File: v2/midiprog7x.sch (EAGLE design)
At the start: 58 parts, among them IC1 PIC18F4550_40, IC2 TPIC6B596N, IC3 78L05Z, IC4 TPIC6B596N, Q1 8MHz, Q2 2N2222A, Q3 2N2222A, Q4 2N2222A

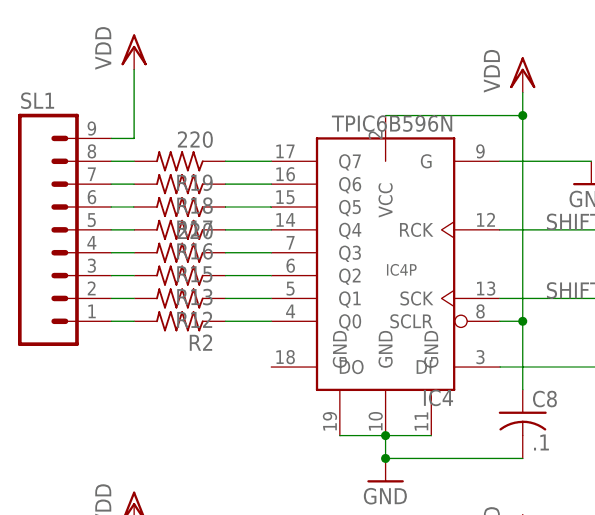
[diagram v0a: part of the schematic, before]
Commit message: Added resistor values.
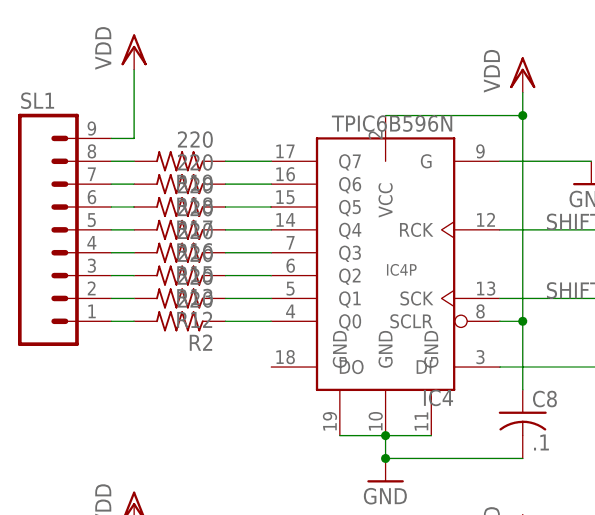
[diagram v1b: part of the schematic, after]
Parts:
- R12, R13, R16, R17, R18, R2: value (none) -> 220
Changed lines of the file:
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@@
 <part name="VDD8" library="supply1" deviceset="VDD" device=""/>
 <part name="GND10" library="supply1" deviceset="GND" device=""/>
-<part name="R2" library="rcl" deviceset="R-US_" device="0207/10"/>
-<part name="R12" library="rcl" deviceset="R-US_" device="0207/10"/>
-<part name="R13" library="rcl" deviceset="R-US_" device="0207/10"/>
+<part name="R2" library="rcl" deviceset="R-US_" device="0207/10" value="220"/>
+<part name="R12" library="rcl" deviceset="R-US_" device="0207/10" value="220"/>
+<part name="R13" library="rcl" deviceset="R-US_" device="0207/10" value="220"/>
 <part name="R15" library="rcl" deviceset="R-US_" device="0207/10" value="220"/>
 <part name="GND14" library="supply1" deviceset="GND" device=""/>
 <part name="C8" library="rcl" deviceset="C-US" device="050-025X075" value=".1"/>
 <part name="VDD12" library="supply1" deviceset="VDD" device=""/>
-<part name="R16" library="rcl" deviceset="R-US_" device="0207/10"/>
-<part name="R17" library="rcl" deviceset="R-US_" device="0207/10"/>
-<part name="R18" library="rcl" deviceset="R-US_" device="0207/10"/>
+<part name="R16" library="rcl" deviceset="R-US_" device="0207/10" value="220"/>
+<part name="R17" library="rcl" deviceset="R-US_" device="0207/10" value="220"/>
+<part name="R18" library="rcl" deviceset="R-US_" device="0207/10" value="220"/>
 <part name="R19" library="rcl" deviceset="R-US_" device="0207/10" value="220"/>
 <part name="R20" library="rcl" deviceset="R-US_" device="0207/10"/>

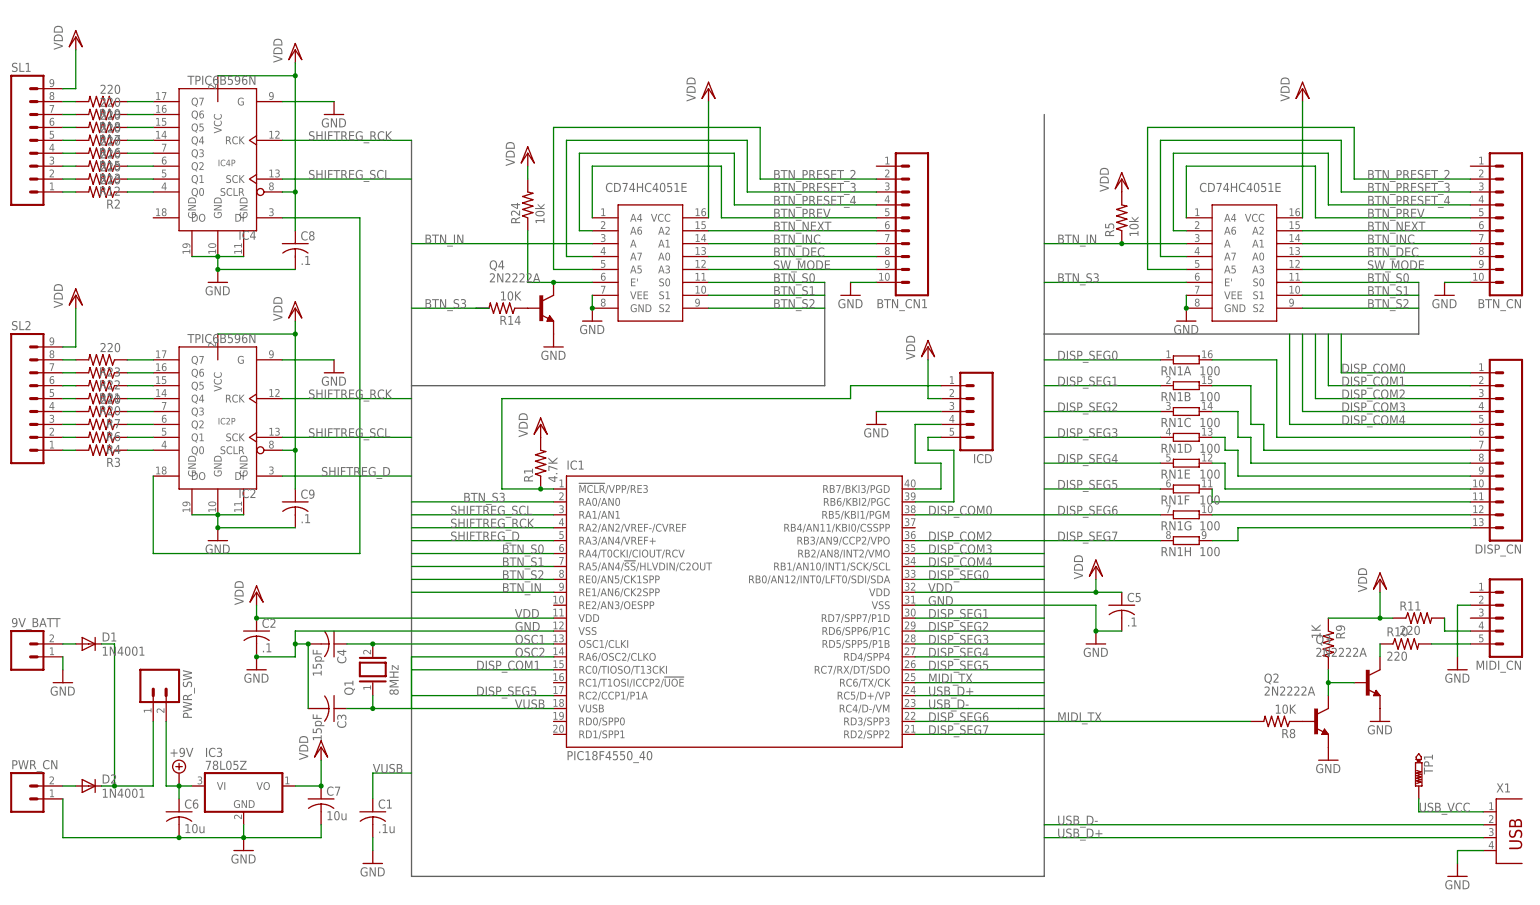
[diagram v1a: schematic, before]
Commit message: Removed busses; corrected names on button inputs; fixed almost all ERC errors.
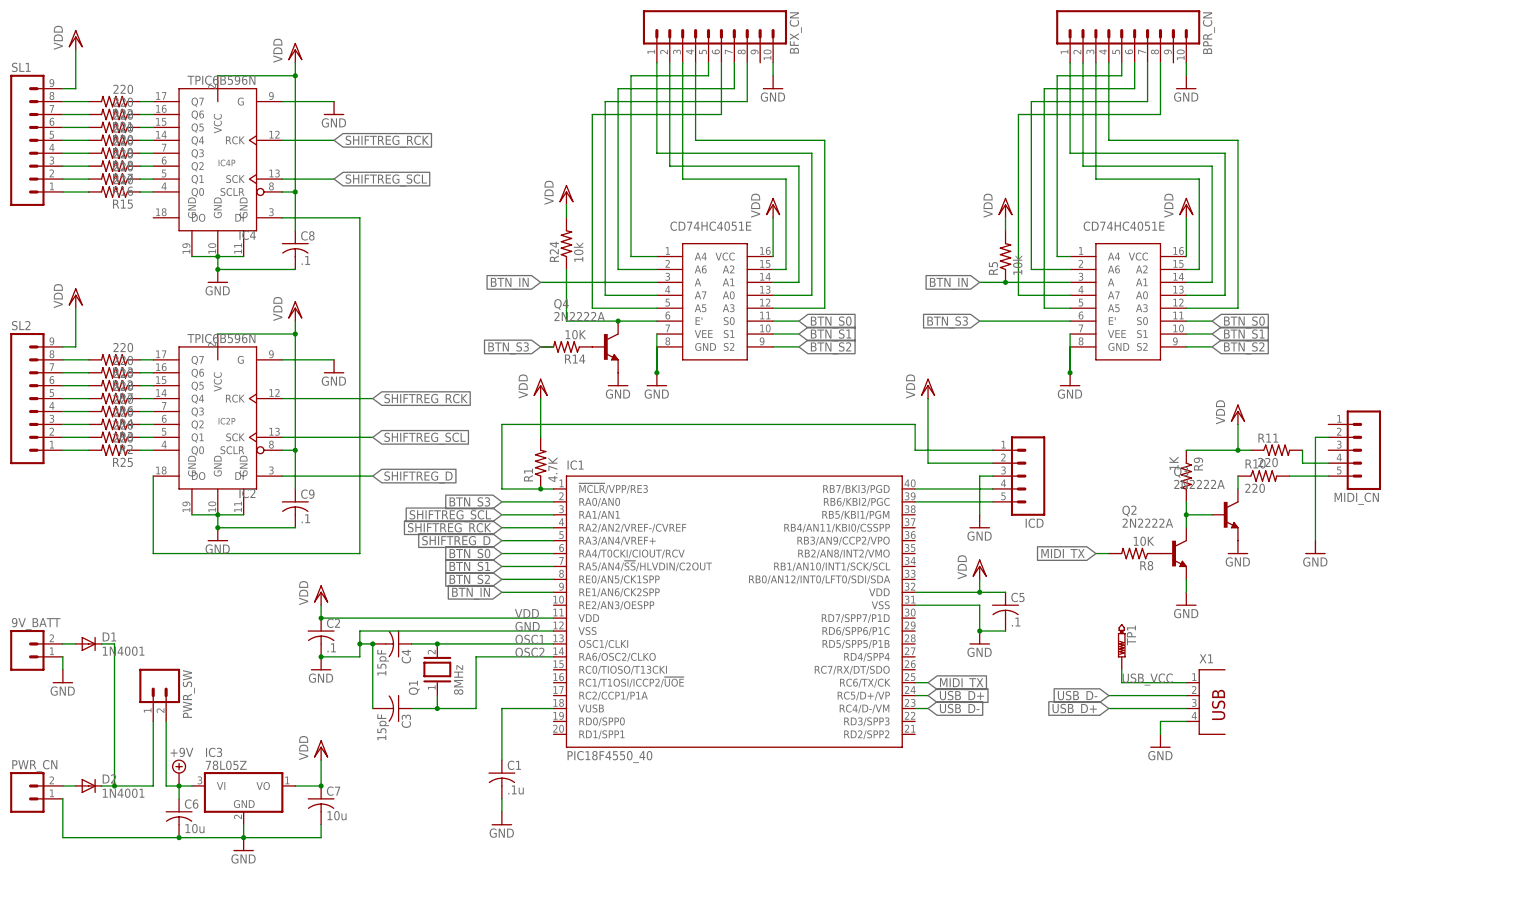
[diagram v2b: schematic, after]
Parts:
- removed BTN_CN, BTN_CN1: (no value), con-amp-quick:M10
- removed DISP_CN: (no value), con-amp-quick:M13
- removed R23: 220, rcl:R-US_0207/10
- removed RN1: 100, resistor-dil:8R-N
- added BFX_CN, BPR_CN: (no value), con-amp-quick:M10
- added R25: 220, rcl:R-US_0207/10
- R20, R21, R22, R3, R4, R6: value (none) -> 220
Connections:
- net VUSB renamed N$18
- removed net BTN_DEC: BTN_CN.8, BTN_CN1.8, U$1.A0, U$2.A0
- removed net BTN_INC: BTN_CN.7, BTN_CN1.7, U$1.A1, U$2.A1
- removed net BTN_NEXT: BTN_CN.6, BTN_CN1.6, U$1.A2, U$2.A2
- removed net BTN_PRESET_2: BTN_CN.2, BTN_CN1.2, U$1.A5, U$2.A5
- removed net BTN_PRESET_3: BTN_CN.3, BTN_CN1.3, U$1.A7, U$2.A7
- removed net BTN_PRESET_4: BTN_CN.4, BTN_CN1.4, U$1.A6, U$2.A6
- removed net BTN_PREV: BTN_CN.5, BTN_CN1.5, U$1.A4, U$2.A4
- removed net DISP_COM0: DISP_CN.1, IC1.RB5/KBI1/PGM
- removed net DISP_COM1: DISP_CN.2, IC1.RC0/TIOSO/T13CKI
- removed net DISP_COM2: DISP_CN.3, IC1.RB3/AN9/CCP2/VPO
- removed net DISP_COM3: DISP_CN.4, IC1.RB2/AN8/INT2/VMO
- removed net DISP_COM4: DISP_CN.5, IC1.RB1/AN10/INT1/SCK/SCL
- removed net DISP_SEG0: IC1.RB0/AN12/INT0/LFT0/SDI/SDA, RN1A.1
- removed net DISP_SEG1: IC1.RD7/SPP7/P1D, RN1B.1
- removed net DISP_SEG2: IC1.RD6/SPP6/P1C, RN1C.1
- removed net DISP_SEG3: IC1.RD5/SPP5/P1B, RN1D.1
- removed net DISP_SEG4: IC1.RD4/SPP4, RN1E.1
- removed net DISP_SEG5: IC1.RC2/CCP1/P1A, IC1.RC7/RX/DT/SDO, RN1F.1
- removed net DISP_SEG6: IC1.RD3/SPP3, RN1G.1
- removed net DISP_SEG7: IC1.RD2/SPP2, RN1H.1
- removed net N$16 (its old number): DISP_CN.13, RN1H.2
- removed net N$17 (its old number): DISP_CN.12, RN1G.2
- removed net N$18 (its old number): DISP_CN.11, RN1F.2
- removed net N$46: R20.1
- removed net N$47: R21.1
- removed net N$48: R22.1
- removed net N$49: R23.1
- removed net N$50: R23.2, SL2.8
- removed net SW_MODE: BTN_CN.9, BTN_CN1.9, U$1.A3, U$2.A3
- new net BFX1: BFX_CN.1, U$2.A0
- new net BFX2: BFX_CN.2, U$2.A1
- new net BFX3: BFX_CN.3, U$2.A2
- new net BFX4: BFX_CN.4, U$2.A3
- new net BFX5: BFX_CN.5, U$2.A4
- new net BFX6: BFX_CN.6, U$2.A5
- new net BFX7: BFX_CN.7, U$2.A6
- new net BFX8: BFX_CN.8, U$2.A7
- new net BPR1: BPR_CN.1, U$1.A0
- new net BPR2: BPR_CN.2, U$1.A1
- new net BPR3: BPR_CN.3, U$1.A2
- new net BPR4: BPR_CN.4, U$1.A3
- new net BPR5: BPR_CN.5, U$1.A4
- new net BPR6: BPR_CN.6, U$1.A5
- new net BPR7: BPR_CN.7, U$1.A6
- new net BPR8: BPR_CN.8, U$1.A7
- net GND: now also BFX_CN.10, BPR_CN.10; no longer BTN_CN.10, BTN_CN1.10
- net N$10: now also IC4G$1.Q6, R21.1; no longer R12.2, SL1.2
- net N$11: now also R21.2, SL1.7; no longer R13.2, SL1.3
- net N$12: now also R20.2, SL1.6; no longer IC4G$1.Q0, R2.1
- net N$13: now also IC4G$1.Q5, R20.1; no longer IC4G$1.Q1, R12.1
- net N$14: now also IC4G$1.Q4, R19.1; no longer IC4G$1.Q2, R13.1
- net N$15: now also R18.1; no longer R15.1
- net N$19: now also R19.2, SL1.5; no longer DISP_CN.10, RN1E.2
- net N$2: now also R22.2, SL1.8; no longer R2.2, SL1.1
- net N$20: now also R18.2, SL1.4; no longer DISP_CN.9, RN1D.2
- net N$21: now also R17.2, SL1.3; no longer DISP_CN.8, RN1C.2
- net N$22: now also R16.2, SL1.2; no longer DISP_CN.7, RN1B.2
- net N$23: now also R15.2, SL1.1; no longer DISP_CN.6, RN1A.2
- net N$24: now also R12.2, SL2.7; no longer R4.2, SL2.2
- net N$25: now also IC4G$1.Q0, R15.1; no longer IC2G$1.Q1, R4.1
- net N$26: now also IC4G$1.Q1, R16.1; no longer IC2G$1.Q2, R6.1
- net N$27: now also R7.2, SL2.6; no longer R6.2, SL2.3
- net N$28: now also R6.2, SL2.5; no longer R7.2, SL2.4
- net N$29: now also IC4G$1.Q2, R17.1; no longer IC2G$1.Q3, R7.1
- net N$3: now also IC4G$1.Q7, R22.1; no longer IC2G$1.Q0, R3.1
- net N$30: now also R4.2, SL2.4; no longer R15.2, SL1.4
- net N$32: now also R3.2, SL2.3; no longer R16.2, SL1.5
- net N$36: now also R2.2, SL2.2; no longer R17.2, SL1.6
- net N$37: now also R25.2, SL2.1; no longer R18.2, SL1.7
- net N$38: now also IC2G$1.Q7, R13.1; no longer R16.1
- net N$39: now also IC2G$1.Q6, R12.1; no longer R17.1
- net N$40: now also IC2G$1.Q5, R7.1; no longer R18.1
- net N$41: now also IC2G$1.Q4, R6.1; no longer R19.1
- net N$42: now also IC2G$1.Q3, R4.1; no longer R19.2, SL1.8
- net N$43: now also IC2G$1.Q2, R3.1; no longer R20.2, SL2.5
- net N$44: now also IC2G$1.Q1, R2.1; no longer R21.2, SL2.6
- net N$45: now also IC2G$1.Q0, R25.1; no longer R22.2, SL2.7
- net N$6: now also R13.2, SL2.8; no longer R3.2, SL2.1
- net VDD: now also SL2.9
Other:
- moved on the sheet: C1, C2, C3, C4, C5, ICD, MIDI_CN, Q1, Q2, Q3, Q4, R10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
